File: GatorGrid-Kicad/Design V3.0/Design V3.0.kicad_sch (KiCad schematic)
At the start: 29 parts, among them J1 Battery-Connector, J2 Conn_01x20_Pin, J3 Conn_01x20_Pin, J4 Conn_01x20_Pin, J5 Conn_01x20_Pin, Q3 2N3904, Q4 2N3904, SW1 SW_SPST, U1 TP4056

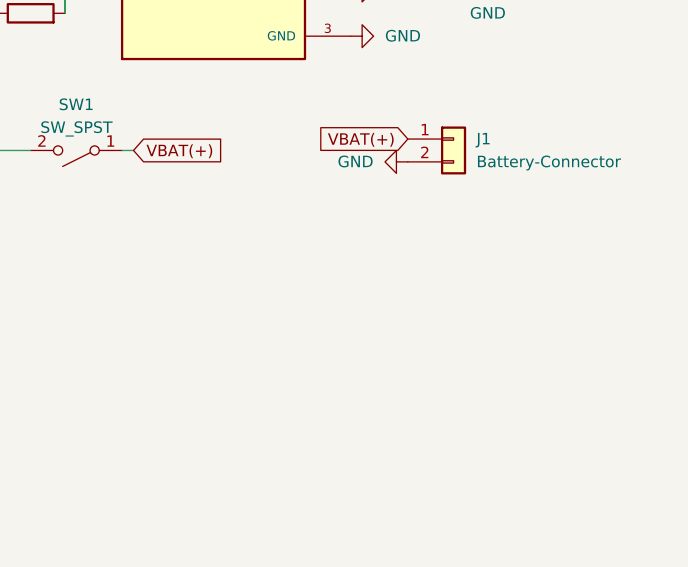
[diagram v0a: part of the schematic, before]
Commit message: added an additional screw for an addition of a sensor PCB
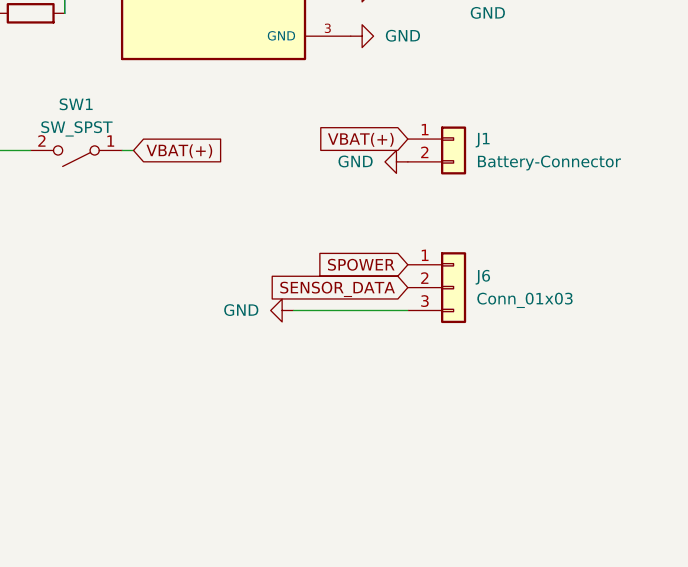
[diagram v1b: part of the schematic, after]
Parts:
- added J6: Conn_01x03, symbol Connector_Generic:Conn_01x03
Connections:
- net GND: now also J6.3 (Pin_3)
- new net SENSOR_DATA: J6.2 (Pin_2)
- new net SPOWER: J6.1 (Pin_1)
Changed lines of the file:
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@@
 	(wire
 		(pts
+			(xy 241.3 151.13) (xy 254 151.13)
+		)
+		(stroke
+			(width 0)
+			(type default)
+		)
+	)
+	(wire
+		(pts
 			(xy 204.47 133.35) (xy 212.09 133.35)
 		)
@@
 		)
 	)
+	(global_label "SENSOR_DATA"
+		(shape input)
+		(at 254 148.59 180)
+		(fields_autoplaced yes)
+		(effects
+			(font
+				(size 1.27 1.27)
+			)
+			(justify right)
+		)
+		(property "Intersheetrefs" "${INTERSHEET_REFS}"
+			(at 238.1334 148.59 0)
+			(effects
+				(font
+					(size 1.27 1.27)
+				)
+				(justify right)
+				(hide yes)
+			)
+		)
+	)
 	(global_label "A_GPIO8"
 		(shape input)
@@
 		)
 	)
+	(global_label "SPOWER"
+		(shape input)
+		(at 254 146.05 180)
+		(fields_autoplaced yes)
+		(effects
+			(font
+				(size 1.27 1.27)
+			)
+			(justify right)
+		)
+		(property "Intersheetrefs" "${INTERSHEET_REFS}"
+			(at 243.3344 146.05 0)
+			(effects
+				(font
+					(size 1.27 1.27)
+				)
+				(justify right)
+				(hide yes)
+			)
+		)
+	)
 	(global_label "A_GPIO2"
 		(shape input)
@@
 	)
 	(symbol
+		(lib_id "power:GND")
+		(at 241.3 151.13 270)
+		(unit 1)
+		(exclude_from_sim no)
+		(in_bom yes)
+		(on_board yes)
+		(dnp no)
+		(fields_autoplaced yes)
+		(property "Reference" "#PWR034"
+			(at 234.95 151.13 0)
+			(effects
+				(font
+					(size 1.27 1.27)
+				)
+				(hide yes)
+			)
+		)
+		(property "Value" "GND"
+			(at 237.49 151.1299 90)
+			(effects
+				(font
+					(size 1.27 1.27)
+				)
+				(justify right)
+			)
+		)
+		(property "Footprint" ""
+			(at 241.3 151.13 0)
+			(effects
+				(font
+					(size 1.27 1.27)
+				)
+				(hide yes)
+			)
+		)
+		(property "Datasheet" ""
+			(at 241.3 151.13 0)
+			(effects
+				(font
+					(size 1.27 1.27)
+				)
+				(hide yes)
+			)
+		)
+		(property "Description" "Power symbol creates a global label with name \"GND\" , ground"
+			(at 241.3 151.13 0)
+			(effects
+				(font
+					(size 1.27 1.27)
+				)
+				(hide yes)
+			)
+		)
+		(pin "1"
+		)
+		(instances
+			(project "Design V3.0"
+				(path "/e5d91564-edf1-47a0-9cf2-4d1020567cc1"
+					(reference "#PWR034")
+					(unit 1)
+				)
+			)
+		)
+	)
+	(symbol
 		(lib_id "MCU_Module:RaspberryPi_Pico")
 		(at 135.89 82.55 0)
@@
 					(unit 1)
 				)
+			)
+		)
+	)
+	(symbol
+		(lib_id "Connector_Generic:Conn_01x03")
+		(at 259.08 148.59 0)
+		(unit 1)
+		(exclude_from_sim no)
+		(in_bom yes)
+		(on_board yes)
+		(dnp no)
+		(fields_autoplaced yes)
+		(property "Reference" "J6"
+			(at 261.62 147.3199 0)
+			(effects
+				(font
+					(size 1.27 1.27)
+				)
+				(justify left)
+			)
+		)
+		(property "Value" "Conn_01x03"
+			(at 261.62 149.8599 0)
+			(effects
+				(font
+					(size 1.27 1.27)
+				)
+				(justify left)
+			)
+		)
+		(property "Footprint" ""
+			(at 259.08 148.59 0)
+			(effects
+				(font
+					(size 1.27 1.27)
+				)
+				(hide yes)
+			)
+		)
+		(property "Datasheet" "~"
+			(at 259.08 148.59 0)
+			(effects
+				(font
+					(size 1.27 1.27)
+				)
+				(hide yes)
+			)
+		)
+		(property "Description" "Generic connector, single row, 01x03, script generated (kicad-library-utils/schlib/autogen/connector/)"
+			(at 259.08 148.59 0)
+			(effects
+				(font
+					(size 1.27 1.27)
+				)
+				(hide yes)
+			)
+		)
+		(pin "1"
+		)
+		(pin "2"
+		)
+		(pin "3"
+		)
+		(instances
+			(project ""
+				(path "/e5d91564-edf1-47a0-9cf2-4d1020567cc1"
+					(reference "J6")
+					(unit 1)
+				)

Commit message: Finalized V3.0
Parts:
- removed J6: Conn_01x03, symbol Connector_Generic:Conn_01x03
- added J7: Conn_01x03, Connector_PinHeader_2.54mm:PinHeader_1x03_P2.54mm_Vertical, symbol Connector_Generic:Conn_01x03
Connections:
- net A_GPIO22 is gone; now on net SENSOR_DATA: A1.29 (GPIO22), J3.12 (Pin_12)
- net A_3V3(OUT): now also J7.2 (Pin_2)
- net GND: now also J7.3 (Pin_3)
- net SENSOR_DATA: now also J7.1 (Pin_1)
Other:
- note added: "3.3V Sensor - GPIO22"

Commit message: Finished V3
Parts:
- A1: value A-RPICO-AP -> A-RPICO-STA
- A2: value B-RPICO-STA -> B-RPICO-AP
- J2, J3, J4, J5: symbol Connector:Conn_01x20_Pin -> Connector_Generic:Conn_01x20
- J7: footprint Connector_PinHeader_2.54mm:PinHeader_1x03_P2.54mm_Vertical -> Connector_JST:JST_XH_S3B-XH-A_1x03_P2.50mm_Horizontal
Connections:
- net A-VBUS: now also J3.20 (Pin_20); no longer J3.1 (Pin_1)
- net A_3V3(OUT): now also J3.16 (Pin_16), J7.1 (Pin_1); no longer J3.5 (Pin_5), J7.2 (Pin_2)
- net A_3V3_EN: now also J3.17 (Pin_17); no longer J3.4 (Pin_4)
- net A_ADC_VREF: now also J3.15 (Pin_15); no longer J3.6 (Pin_6)
- net A_GPIO0: now also J2.1 (Pin_1); no longer J2.20 (Pin_20)
- net A_GPIO1: now also J2.2 (Pin_2); no longer J2.19 (Pin_19)
- net A_GPIO10: now also J2.14 (Pin_14); no longer J2.7 (Pin_7)
- net A_GPIO11: now also J2.15 (Pin_15); no longer J2.6 (Pin_6)
- net A_GPIO14: now also J2.19 (Pin_19); no longer J2.2 (Pin_2)
- net A_GPIO15: now also J2.20 (Pin_20); no longer J2.1 (Pin_1)
- net A_GPIO2: now also J2.4 (Pin_4); no longer J2.17 (Pin_17)
- net A_GPIO20: now also J3.6 (Pin_6); no longer J3.15 (Pin_15)
- net A_GPIO21: now also J3.7 (Pin_7); no longer J3.14 (Pin_14)
- net A_GPIO26: now also J3.11 (Pin_11); no longer J3.10 (Pin_10)
- net A_GPIO27: now also J3.12 (Pin_12); no longer J3.9 (Pin_9)
- net A_GPIO28: now also J3.14 (Pin_14); no longer J3.7 (Pin_7)
- net A_GPIO3: now also J2.5 (Pin_5); no longer J2.16 (Pin_16)
- net A_GPIO4: now also J2.6 (Pin_6); no longer J2.15 (Pin_15)
- net A_GPIO5: now also J2.7 (Pin_7); no longer J2.14 (Pin_14)
- net A_GPIO6: now also J2.9 (Pin_9); no longer J2.12 (Pin_12)
- net A_GPIO7: now also J2.10 (Pin_10); no longer J2.11 (Pin_11)
- net A_GPIO8: now also J2.11 (Pin_11); no longer J2.10 (Pin_10)
- net A_GPIO9: now also J2.12 (Pin_12); no longer J2.9 (Pin_9)
- net A_RUN: now also J3.10 (Pin_10); no longer J3.11 (Pin_11)
- net B-VBUS: now also J5.20 (Pin_20); no longer J5.1 (Pin_1)
- net B_3V3(OUT): now also J5.16 (Pin_16); no longer J5.5 (Pin_5)
- net B_3V3_EN: now also J5.17 (Pin_17); no longer J5.4 (Pin_4)
- net B_ADC_VREF: now also J5.15 (Pin_15); no longer J5.6 (Pin_6)
- net B_GPIO0: now also J4.1 (Pin_1); no longer J4.20 (Pin_20)
- net B_GPIO1: now also J4.2 (Pin_2); no longer J4.19 (Pin_19)
- net B_GPIO10: now also J4.14 (Pin_14); no longer J4.7 (Pin_7)
- net B_GPIO11: now also J4.15 (Pin_15); no longer J4.6 (Pin_6)
- net B_GPIO14: now also J4.19 (Pin_19); no longer J4.2 (Pin_2)
- net B_GPIO15: now also J4.20 (Pin_20); no longer J4.1 (Pin_1)
- net B_GPIO2: now also J4.4 (Pin_4); no longer J4.17 (Pin_17)
- net B_GPIO20: now also J5.6 (Pin_6); no longer J5.15 (Pin_15)
- net B_GPIO21: now also J5.7 (Pin_7); no longer J5.14 (Pin_14)
- net B_GPIO22: now also J5.9 (Pin_9); no longer J5.12 (Pin_12)
- net B_GPIO26: now also J5.11 (Pin_11); no longer J5.10 (Pin_10)
- net B_GPIO27: now also J5.12 (Pin_12); no longer J5.9 (Pin_9)
- net B_GPIO28: now also J5.14 (Pin_14); no longer J5.7 (Pin_7)
- net B_GPIO3: now also J4.5 (Pin_5); no longer J4.16 (Pin_16)
- net B_GPIO4: now also J4.6 (Pin_6); no longer J4.15 (Pin_15)
- net B_GPIO5: now also J4.7 (Pin_7); no longer J4.14 (Pin_14)
- net B_GPIO6: now also J4.9 (Pin_9); no longer J4.12 (Pin_12)
- net B_GPIO7: now also J4.10 (Pin_10); no longer J4.11 (Pin_11)
- net B_GPIO8: now also J4.11 (Pin_11); no longer J4.10 (Pin_10)
- net B_GPIO9: now also J4.12 (Pin_12); no longer J4.9 (Pin_9)
- net B_RUN: now also J5.10 (Pin_10); no longer J5.11 (Pin_11)
- net CS: now also J3.2 (Pin_2), J5.2 (Pin_2); no longer J3.19 (Pin_19), J5.19 (Pin_19)
- net RX-TX: now also J3.1 (Pin_1), J5.5 (Pin_5); no longer J3.20 (Pin_20), J5.16 (Pin_16)
- net SCK: now also J3.4 (Pin_4), J5.4 (Pin_4); no longer J3.17 (Pin_17), J5.17 (Pin_17)
- net SENSOR_DATA: now also J3.9 (Pin_9), J7.2 (Pin_2); no longer J3.12 (Pin_12), J7.1 (Pin_1)
- net TX-RX: now also J3.5 (Pin_5), J5.1 (Pin_1); no longer J3.16 (Pin_16), J5.20 (Pin_20)
- net UART_RX: now also J2.17 (Pin_17), J4.16 (Pin_16); no longer J2.4 (Pin_4), J4.5 (Pin_5)
- net UART_TX: now also J2.16 (Pin_16), J4.17 (Pin_17); no longer J2.5 (Pin_5), J4.4 (Pin_4)
- net VSYS: now also J3.19 (Pin_19), J5.19 (Pin_19); no longer J3.2 (Pin_2), J5.2 (Pin_2)
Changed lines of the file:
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@@
 	(global_label "A_3V3(OUT)"
 		(shape input)
-		(at 257.81 151.13 180)
+		(at 257.81 148.59 180)
 		(fields_autoplaced yes)
 		(effects
@@
 		)
 		(property "Intersheetrefs" "${INTERSHEET_REFS}"
-			(at 243.939 151.13 0)
+			(at 243.939 148.59 0)
 			(effects
 				(font
@@
 	(global_label "SENSOR_DATA"
 		(shape input)
-		(at 257.81 148.59 180)
+		(at 257.81 151.13 180)
 		(fields_autoplaced yes)
 		(effects
@@
 		)
 		(property "Intersheetrefs" "${INTERSHEET_REFS}"
-			(at 241.9434 148.59 0)
+			(at 241.9434 151.13 0)
 			(effects
 				(font
@@
 			)
 		)
-		(property "Value" "B-RPICO-STA"
+		(property "Value" "B-RPICO-AP"
 			(at 138.0333 119.38 0)
 			(effects
@@
 			)
 		)
-		(property "Value" "A-RPICO-AP"
+		(property "Value" "A-RPICO-STA"
 			(at 54.2133 119.38 0)
 			(effects
@@
 	)
 	(symbol
-		(lib_id "Connector:Conn_01x20_Pin")
-		(at 143.51 156.21 0)
+		(lib_id "Connector_Generic:Conn_01x20")
+		(at 143.51 158.75 180)
 		(unit 1)
 		(exclude_from_sim no)
@@
 		(dnp no)
 		(property "Reference" "J5"
-			(at 145.542 129.286 0)
+			(at 141.478 185.674 0)
 			(effects
 				(font
@@
 		)
 		(property "Value" "Conn_01x20_Pin"
-			(at 146.304 185.166 0)
+			(at 140.716 129.794 0)
 			(effects
 				(font
@@
 		)
 		(property "Footprint" "Connector_PinSocket_2.54mm:PinSocket_1x20_P2.54mm_Vertical"
-			(at 143.51 156.21 0)
+			(at 143.51 158.75 0)
 			(effects
 				(font
@@
 		)
 		(property "Datasheet" "~"
-			(at 143.51 156.21 0)
+			(at 143.51 158.75 0)
 			(effects
 				(font
@@
 			)
 		)
-		(property "Description" "Generic connector, single row, 01x20, script generated"
-			(at 143.51 156.21 0)
+		(property "Description" "Generic connector, single row, 01x20, script generated (kicad-library-utils/schlib/autogen/connector/)"
+			(at 143.51 158.75 0)
 			(effects
 				(font
@@
 	)
 	(symbol
-		(lib_id "Connector:Conn_01x20_Pin")
-		(at 44.45 157.48 180)
+		(lib_id "Connector_Generic:Conn_01x20")
+		(at 44.45 154.94 0)
 		(unit 1)
 		(exclude_from_sim no)
@@
 		(dnp no)
 		(property "Reference" "J2"
-			(at 40.894 127.254 0)
+			(at 48.006 185.166 0)
 			(effects
 				(font
@@
 		)
 		(property "Value" "Conn_01x20_Pin"
-			(at 35.306 185.166 0)
+			(at 53.594 127.254 0)
 			(effects
 				(font
@@
 		)
 		(property "Footprint" "Connector_PinSocket_2.54mm:PinSocket_1x20_P2.54mm_Vertical"
-			(at 44.45 157.48 0)
+			(at 44.45 154.94 0)
 			(effects
 				(font
@@
 		)
 		(property "Datasheet" "~"
-			(at 44.45 157.48 0)
+			(at 44.45 154.94 0)
 			(effects
 				(font
@@
 			)
 		)
-		(property "Description" "Generic connector, single row, 01x20, script generated"
-			(at 44.45 157.48 0)
+		(property "Description" "Generic connector, single row, 01x20, script generated (kicad-library-utils/schlib/autogen/connector/)"
+			(at 44.45 154.94 0)
 			(effects
 				(font
@@
 	)
 	(symbol
-		(lib_id "Connector:Conn_01x20_Pin")
-		(at 62.23 154.94 0)
+		(lib_id "Connector_Generic:Conn_01x20")
+		(at 62.23 157.48 180)
 		(unit 1)
 		(exclude_from_sim no)
@@
 		(dnp no)
 		(property "Reference" "J3"
-			(at 64.262 128.016 0)
+			(at 60.198 184.404 0)
 			(effects
 				(font
@@
 		)
 		(property "Value" "Conn_01x20_Pin"
-			(at 65.024 183.896 0)
+			(at 59.436 128.524 0)
 			(effects
 				(font
@@
 		)
 		(property "Footprint" "Connector_PinSocket_2.54mm:PinSocket_1x20_P2.54mm_Vertical"
-			(at 62.23 154.94 0)
+			(at 62.23 157.48 0)
 			(effects
 				(font
@@
 		)
 		(property "Datasheet" "~"
-			(at 62.23 154.94 0)
+			(at 62.23 157.48 0)
 			(effects
 				(font
@@
 			)
 		)
-		(property "Description" "Generic connector, single row, 01x20, script generated"
-			(at 62.23 154.94 0)
+		(property "Description" "Generic connector, single row, 01x20, script generated (kicad-library-utils/schlib/autogen/connector/)"
+			(at 62.23 157.48 0)
 			(effects
 				(font
@@
 	)
 	(symbol
-		(lib_id "Connector:Conn_01x20_Pin")
-		(at 125.73 158.75 180)
+		(lib_id "Connector_Generic:Conn_01x20")
+		(at 125.73 156.21 0)
 		(unit 1)
 		(exclude_from_sim no)
@@
 		(dnp no)
 		(property "Reference" "J4"
-			(at 122.174 128.524 0)
+			(at 129.286 186.436 0)
 			(effects
 				(font
@@
 		)
 		(property "Value" "Conn_01x20_Pin"
-			(at 116.586 186.436 0)
+			(at 134.874 128.524 0)
 			(effects
 				(font
@@
 		)
 		(property "Footprint" "Connector_PinSocket_2.54mm:PinSocket_1x20_P2.54mm_Vertical"
-			(at 125.73 158.75 0)
+			(at 125.73 156.21 0)
 			(effects
 				(font
@@
 		)
 		(property "Datasheet" "~"
-			(at 125.73 158.75 0)
+			(at 125.73 156.21 0)
 			(effects
 				(font
@@
 			)
 		)
-		(property "Description" "Generic connector, single row, 01x20, script generated"
-			(at 125.73 158.75 0)
+		(property "Description" "Generic connector, single row, 01x20, script generated (kicad-library-utils/schlib/autogen/connector/)"
+			(at 125.73 156.21 0)
 			(effects
 				(font
@@
 			)
 		)
-		(property "Footprint" "Connector_PinHeader_2.54mm:PinHeader_1x03_P2.54mm_Vertical"
+		(property "Footprint" "Connector_JST:JST_XH_S3B-XH-A_1x03_P2.50mm_Horizontal"
 			(at 262.89 151.13 0)
 			(effects
